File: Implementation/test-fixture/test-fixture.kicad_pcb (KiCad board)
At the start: 2 copper layers, 134.6 x 55.9 mm, 10 parts, among them J1 Conn_02x31_Odd_Even, SW1 SW_Push, SW2 SW_Push

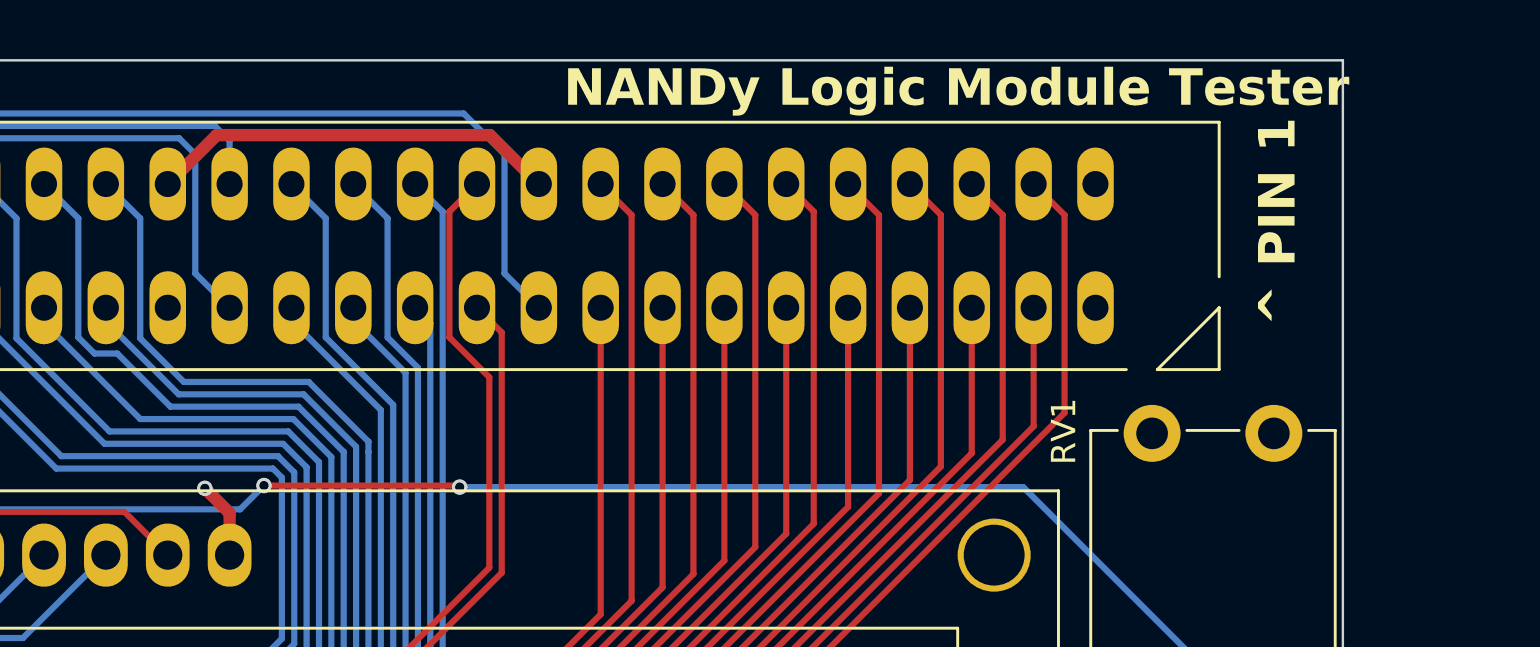
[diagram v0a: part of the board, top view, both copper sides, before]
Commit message: Routed 16C550 serial card
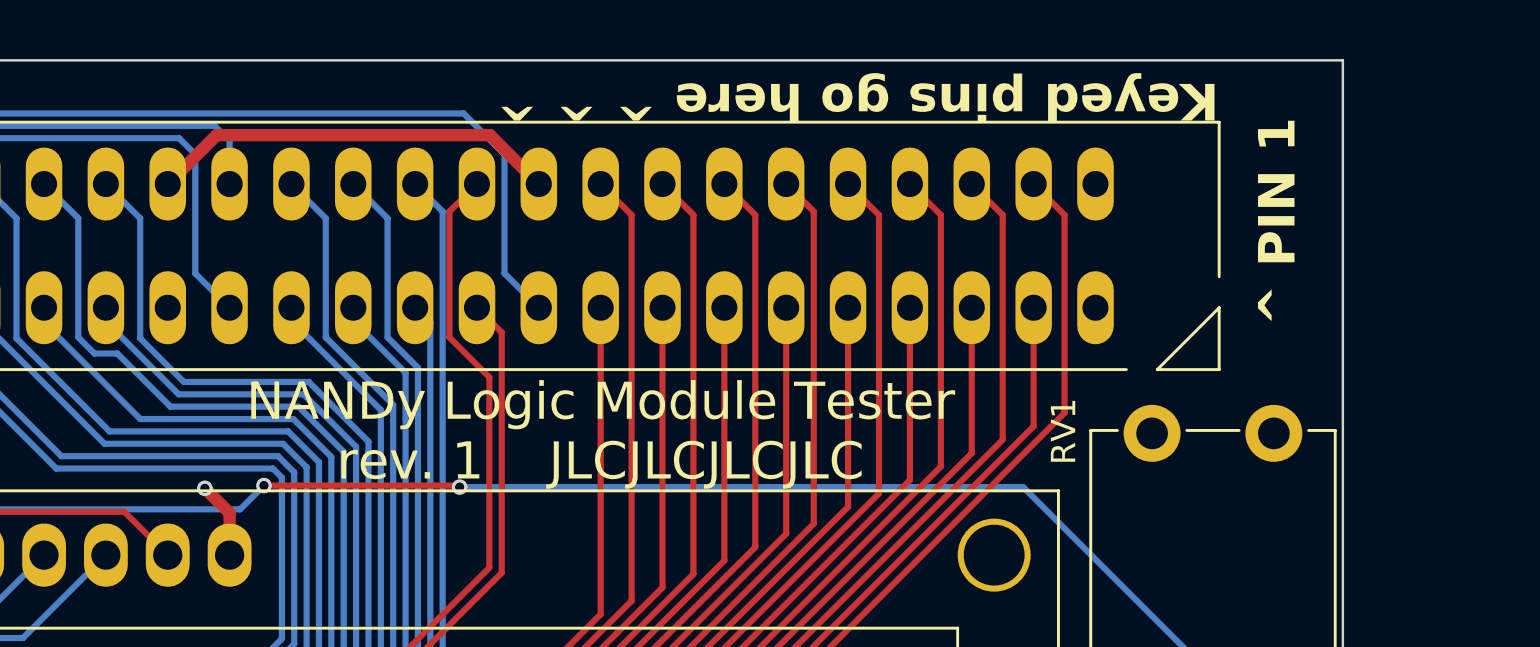
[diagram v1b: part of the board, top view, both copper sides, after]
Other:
- board text added: "Keyed pins go here ^ ^ ^"
- board text added: "NANDy Logic Module Tester rev. 1 JLCJLCJLCJLC"
- board text removed: "NANDy Logic Module Tester"
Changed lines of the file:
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@@
 		)
 	)
-	(gr_text "NANDy Logic Module Tester"
-		(at 168.656 101.854 0)
+	(gr_text "Keyed pins go here ^ ^ ^"
+		(at 195.58 104.14 180)
 		(layer "F.SilkS")
 		(effects
@@
 		)
 	)
+	(gr_text "NANDy Logic Module Tester\nrev. 1    JLCJLCJLCJLC"
+		(at 170.18 116.84 0)
+		(layer "F.SilkS")
+		(effects
+			(font
+				(size 1.524 1.524)
+				(thickness 0.254)
+			)
+		)
+	)
